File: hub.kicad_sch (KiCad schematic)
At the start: 21 parts, among them U201 USB2512B, Y201 24MHz

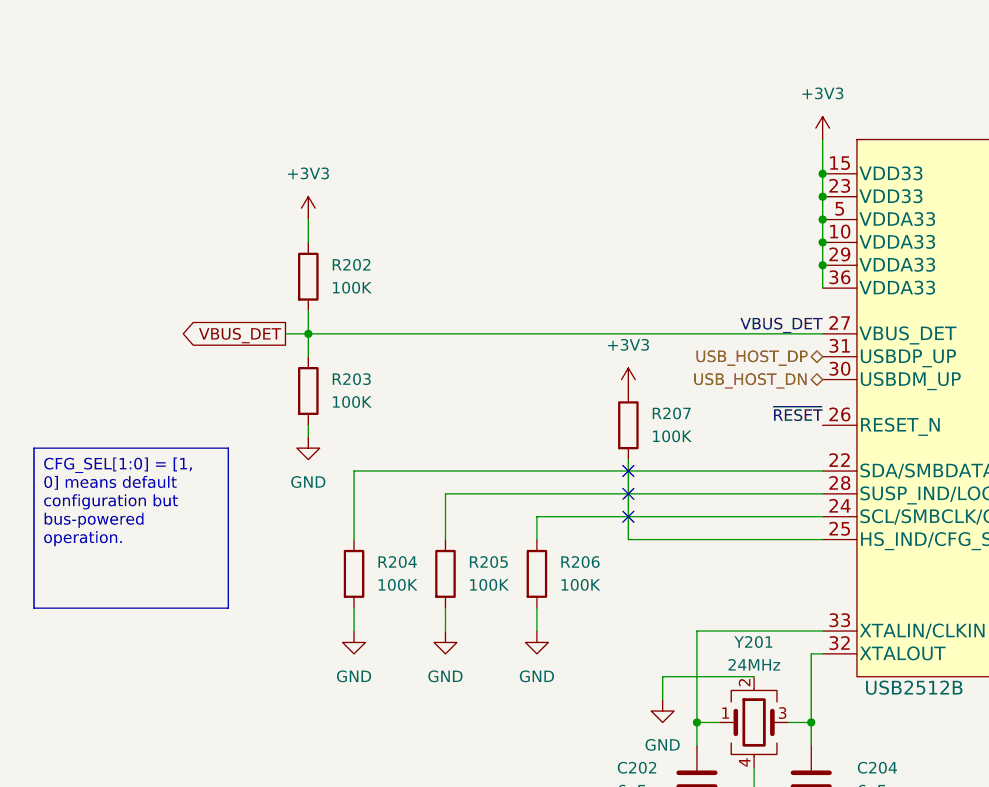
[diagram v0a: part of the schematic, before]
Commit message: Update schematic with feedback
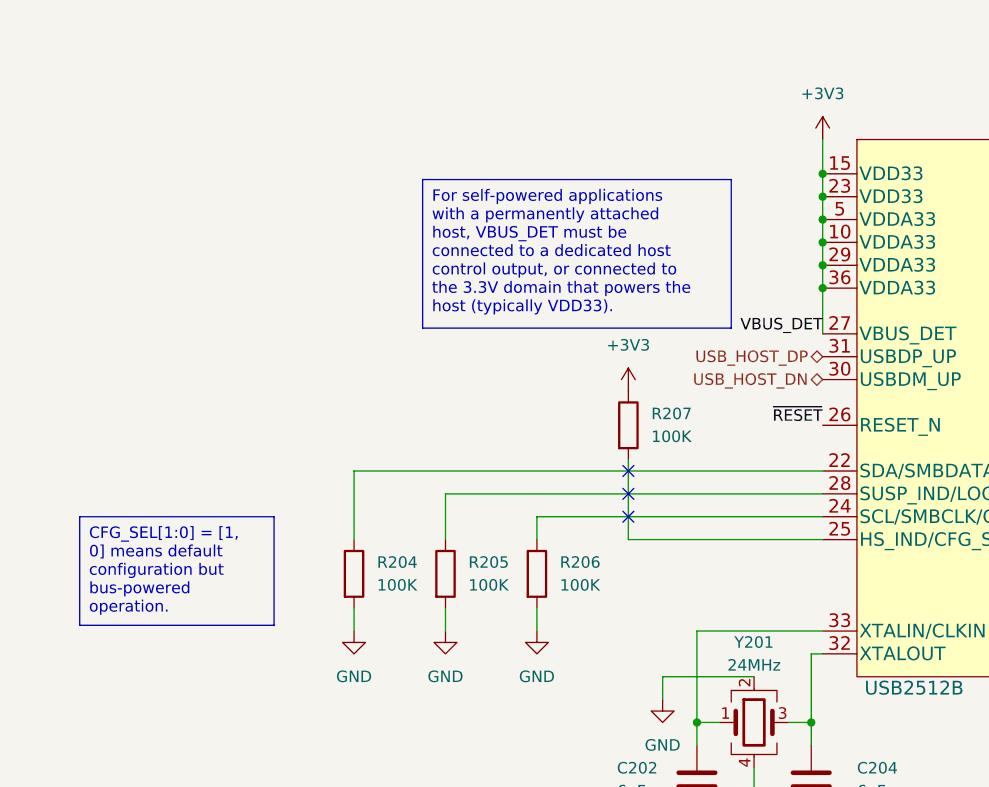
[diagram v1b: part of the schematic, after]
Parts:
- removed R202, R203: 100K, Resistor_SMD:R_0201_0603Metric, symbol Device:R
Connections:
- net VBUS_DET is gone; now on net +3V3: U201.27 (VBUS_DET)
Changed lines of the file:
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@@
   (junction (at 125.73 72.39) (diameter 0) (color 0 0 0 0)
   )
-  (junction (at 68.58 90.17) (diameter 0) (color 0 0 0 0)
-  )
   (junction (at 123.19 41.91) (diameter 0) (color 0 0 0 0)
   )
@@
   )
   (junction (at 109.22 34.29) (diameter 0) (color 0 0 0 0)
+  )
+  (junction (at 125.73 85.09) (diameter 0) (color 0 0 0 0)
   )
   (junction (at 179.07 41.91) (diameter 0) (color 0 0 0 0)
@@
     (stroke (width 0) (type default))
   )
-  (wire (pts (xy 66.04 90.17) (xy 68.58 90.17))
-    (stroke (width 0) (type default))
-  )
   (wire (pts (xy 124.46 143.51) (xy 124.46 146.05))
     (stroke (width 0) (type default))
@@
     (stroke (width 0) (type default))
   )
-  (wire (pts (xy 68.58 100.33) (xy 68.58 101.6))
-    (stroke (width 0) (type default))
-  )
-  (wire (pts (xy 68.58 90.17) (xy 125.73 90.17))
-    (stroke (width 0) (type default))
-  )
   (wire (pts (xy 177.8 118.11) (xy 208.28 118.11))
     (stroke (width 0) (type default))
@@
     (stroke (width 0) (type default))
   )
-  (wire (pts (xy 68.58 77.47) (xy 68.58 80.01))
-    (stroke (width 0) (type default))
-  )
   (wire (pts (xy 177.8 123.19) (xy 184.15 123.19))
     (stroke (width 0) (type default))
@@
     (stroke (width 0) (type default))
   )
+  (wire (pts (xy 125.73 85.09) (xy 125.73 90.17))
+    (stroke (width 0) (type default))
+  )
   (wire (pts (xy 73.66 113.03) (xy 73.66 105.41))
     (stroke (width 0) (type default))
@@
     (stroke (width 0) (type default))
   )
-  (wire (pts (xy 68.58 90.17) (xy 68.58 92.71))
-    (stroke (width 0) (type default))
-  )
   (wire (pts (xy 50.8 176.53) (xy 50.8 177.8))
     (stroke (width 0) (type default))
   )
-  (wire (pts (xy 68.58 87.63) (xy 68.58 90.17))
-    (stroke (width 0) (type default))
-  )
   (wire (pts (xy 194.31 72.39) (xy 177.8 72.39))
     (stroke (width 0) (type default))
   )
-  (text_box "CFG_SEL[1:0] = [1, 0] means default configuration but bus-powered operation."
-    (at 38.1 102.87 0) (size 21.59 17.78)
+  (text_box "For self-powered applications with a permanently attached host, VBUS_DET must be connected to a dedicated host control output, or connected to the 3.3V domain that powers the host (typically VDD33)."
+    (at 81.28 73.025 0) (size 34.29 16.51)
     (stroke (width 0) (type default))
     (fill (type none))
     (effects (font (size 1.27 1.27)) (justify left top))
   )
+  (text_box "CFG_SEL[1:0] = [1, 0] means default configuration but bus-powered operation."
+    (at 43.18 110.49 0) (size 21.59 12.065)
+    (stroke (width 0) (type default))
+    (fill (type none))
+    (effects (font (size 1.27 1.27)) (justify left top))
+  )
   (label "USB_P2_DP" (at 177.8 90.17 0) (fields_autoplaced)
     (effects (font (size 1.27 1.27)) (justify left bottom))
@@
     (effects (font (size 1.27 1.27)) (justify right bottom))
   )
-  (global_label "VBUS_DET" (shape output) (at 66.04 90.17 180) (fields_autoplaced)
-    (effects (font (size 1.27 1.27)) (justify right))
-    (property "Intersheetrefs" "${INTERSHEET_REFS}" (at 54.5356 90.17 0)
-      (effects (font (size 1.27 1.27)) (justify right) hide)
-    )
-  )
   (hierarchical_label "USB_HOST_DP" (shape bidirectional) (at 125.73 92.71 180) (fields_autoplaced)
     (effects (font (size 1.27 1.27)) (justify right))
@@
         (path "/dd4f7be7-d725-4a95-9fbf-108927ba51c4/aa0e66ac-b3de-4886-b605-6f9fbcf97e89"
           (reference "#PWR0318") (unit 1)
-        )
-      )
-    )
-  )
-  (symbol (lib_id "power:GND") (at 68.58 101.6 0) (unit 1)
-    (in_bom yes) (on_board yes) (dnp no) (fields_autoplaced)
-    (property "Reference" "#PWR0303" (at 68.58 107.95 0)
-      (effects (font (size 1.27 1.27)) hide)
-    )
-    (property "Value" "GND" (at 68.58 106.68 0)
-      (effects (font (size 1.27 1.27)))
-    )
-    (property "Footprint" "" (at 68.58 101.6 0)
-      (effects (font (size 1.27 1.27)) hide)
-    )
-    (property "Datasheet" "" (at 68.58 101.6 0)
-      (effects (font (size 1.27 1.27)) hide)
-    )
-    (pin "1")
-    (instances
-      (project "2usbc"
-        (path "/dd4f7be7-d725-4a95-9fbf-108927ba51c4/aa0e66ac-b3de-4886-b605-6f9fbcf97e89"
-          (reference "#PWR0303") (unit 1)
         )
       )
@@
     )
   )
-  (symbol (lib_id "Device:R") (at 68.58 96.52 0) (unit 1)
-    (in_bom yes) (on_board yes) (dnp no) (fields_autoplaced)
-    (property "Reference" "R203" (at 71.12 95.2499 0)
-      (effects (font (size 1.27 1.27)) (justify left))
-    )
-    (property "Value" "100K" (at 71.12 97.7899 0)
-      (effects (font (size 1.27 1.27)) (justify left))
-    )
-    (property "Footprint" "Resistor_SMD:R_0201_0603Metric" (at 66.802 96.52 90)
-      (effects (font (size 1.27 1.27)) hide)
-    )
-    (property "Datasheet" "~" (at 68.58 96.52 0)
-      (effects (font (size 1.27 1.27)) hide)
-    )
-    (pin "1")
-    (pin "2")
-    (instances
-      (project "2usbc"
-        (path "/dd4f7be7-d725-4a95-9fbf-108927ba51c4/aa0e66ac-b3de-4886-b605-6f9fbcf97e89"
-          (reference "R203") (unit 1)
-        )
-      )
-    )
-  )
   (symbol (lib_id "Device:C") (at 111.76 139.7 0) (unit 1)
     (in_bom yes) (on_board yes) (dnp no)
@@
     )
   )
-  (symbol (lib_id "power:+3V3") (at 68.58 77.47 0) (unit 1)
-    (in_bom yes) (on_board yes) (dnp no) (fields_autoplaced)
-    (property "Reference" "#PWR0302" (at 68.58 81.28 0)
-      (effects (font (size 1.27 1.27)) hide)
-    )
-    (property "Value" "+3V3" (at 68.58 72.39 0)
-      (effects (font (size 1.27 1.27)))
-    )
-    (property "Footprint" "" (at 68.58 77.47 0)
-      (effects (font (size 1.27 1.27)) hide)
-    )
-    (property "Datasheet" "" (at 68.58 77.47 0)
-      (effects (font (size 1.27 1.27)) hide)
-    )
-    (pin "1")
-    (instances
-      (project "2usbc"
-        (path "/dd4f7be7-d725-4a95-9fbf-108927ba51c4/aa0e66ac-b3de-4886-b605-6f9fbcf97e89"
-          (reference "#PWR0302") (unit 1)
-        )
-      )
-    )
-  )
   (symbol (lib_id "Device:C") (at 184.15 127 0) (unit 1)
     (in_bom yes) (on_board yes) (dnp no) (fields_autoplaced)
@@
         )
       )
-    )
-  )
-  (symbol (lib_id "Device:R") (at 68.58 83.82 0) (unit 1)
-    (in_bom yes) (on_board yes) (dnp no) (fields_autoplaced)
-    (property "Reference" "R202" (at 71.12 82.5499 0)
-      (effects (font (size 1.27 1.27)) (justify left))
-    )
-    (property "Value" "100K" (at 71.12 85.0899 0)
-      (effects (font (size 1.27 1.27)) (justify left))
-    )
-    (property "Footprint" "Resistor_SMD:R_0201_0603Metric" (at 66.802 83.82 90)
-      (effects (font (size 1.27 1.27)) hide)
-    )
-    (property "Datasheet" "~" (at 68.58 83.82 0)
-      (effects (font (size 1.27 1.27)) hide)
-    )
-    (pin "1")
-    (pin "2")
-    (instances
-      (project "2usbc"
-        (path "/dd4f7be7-d725-4a95-9fbf-108927ba51c4/aa0e66ac-b3de-4886-b605-6f9fbcf97e89"
-          (reference "R202") (unit 1)
-        )
-      )
